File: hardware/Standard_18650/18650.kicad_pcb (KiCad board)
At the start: 2 copper layers, 109.7 x 16 mm, 57 parts, among them J2 Battery, J3 GPIO, J4 USB_B_Micro, J5 Power, J6 LEDs, J7 GPIO, Q1 BSS806N, Q2 BSS806N, Q3 BSS806N, Q4 BSS806N, SW1 Mode, SW2 Power, U1 STM32F412CGUx, U2 AP2210N-3.3TRG1, U3 BQ21040, U4 ESD7002WTT1G, Y1 32.768kHz

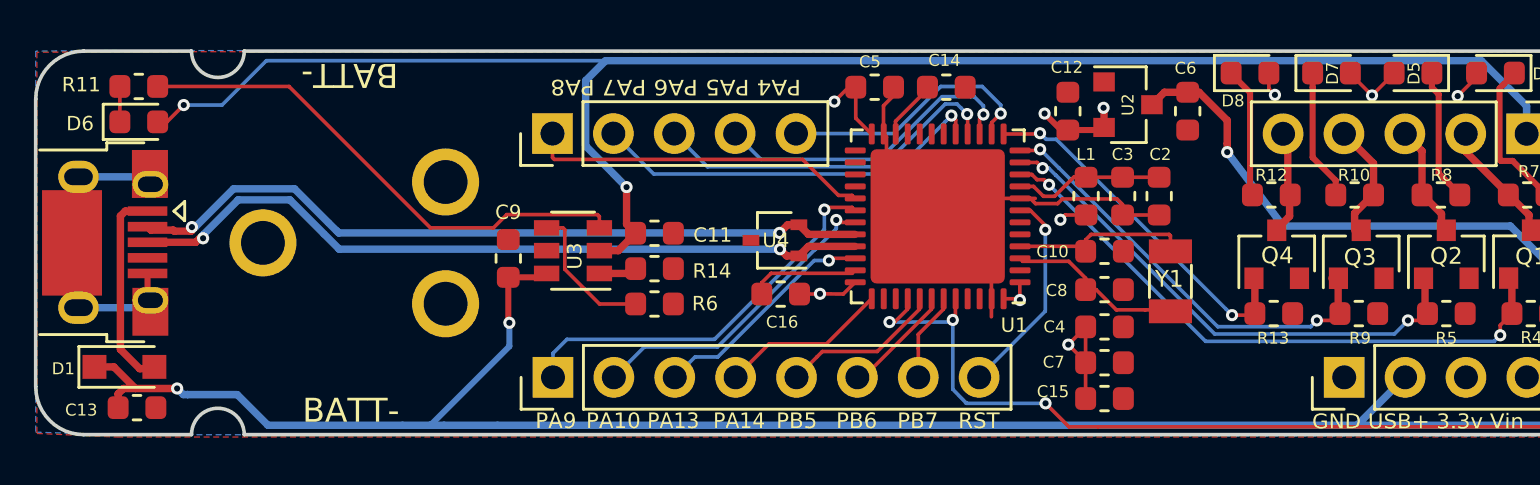
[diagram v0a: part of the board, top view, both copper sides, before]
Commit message: Add HSE crystal
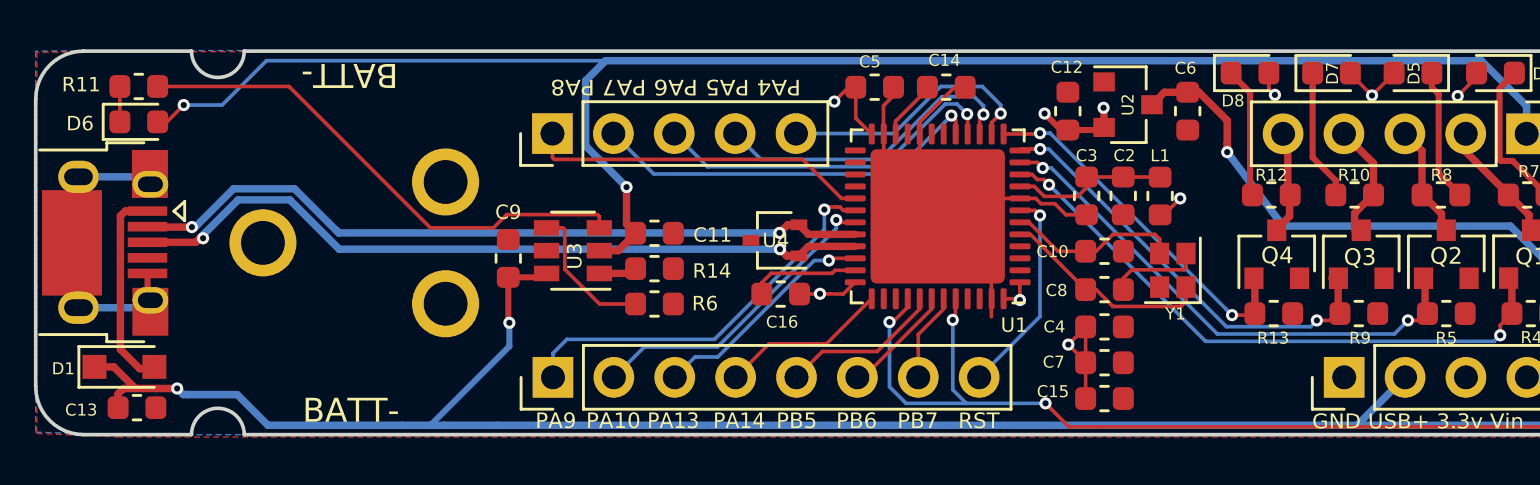
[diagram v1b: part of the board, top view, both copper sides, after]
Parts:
- C10, C8: value 7pF -> 6pF
- C11, C13, C2, C6: value 1uf -> 1uF
- C15, C16, C3, C4, C5: value 100nf -> 100nF
- Y1: value 32.768kHz -> 24Mhz; footprint Crystal:Crystal_SMD_3215-2Pin_3.2x1.5mm -> Crystal:Crystal_SMD_2016-4Pin_2.0x1.6mm
- moved L1 3.09 mm to (105.0, 98.0)
- moved C2 1.50 mm to (103.5, 98.0)
- moved C3 1.50 mm to (101.9, 98.0)
- moved Y1 0.47 mm to (105.5, 101.1), turned to 90 degrees
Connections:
- U1 pad 20: (no net) -> GND
- U1 pad 3: /XTAL1 -> (no net)
- U1 pad 4: /XTAL2 -> (no net)
- U1 pad 5: (no net) -> /XTAL1
- U1 pad 6: (no net) -> /XTAL2
- Y1 pad 2: /XTAL2 -> GND
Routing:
- net GND: track 31.8 -> 41.3 mm
- net /BUTTON: track 40.4 -> 44.0 mm
- net /XTAL1: track 7.45 -> 8.86 mm
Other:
- board text added: "rev 1.1a2"
- board text removed: "rev 1.1a"

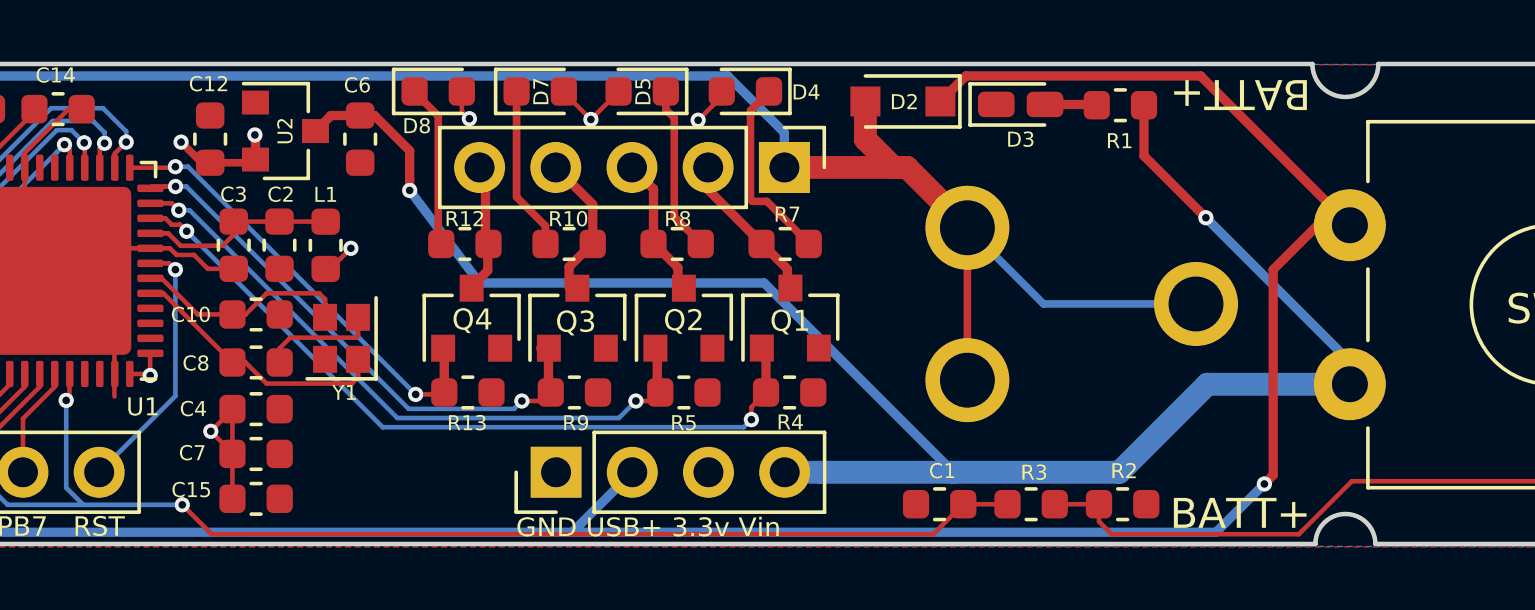
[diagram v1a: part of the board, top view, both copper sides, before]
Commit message: Add extra ground pin.
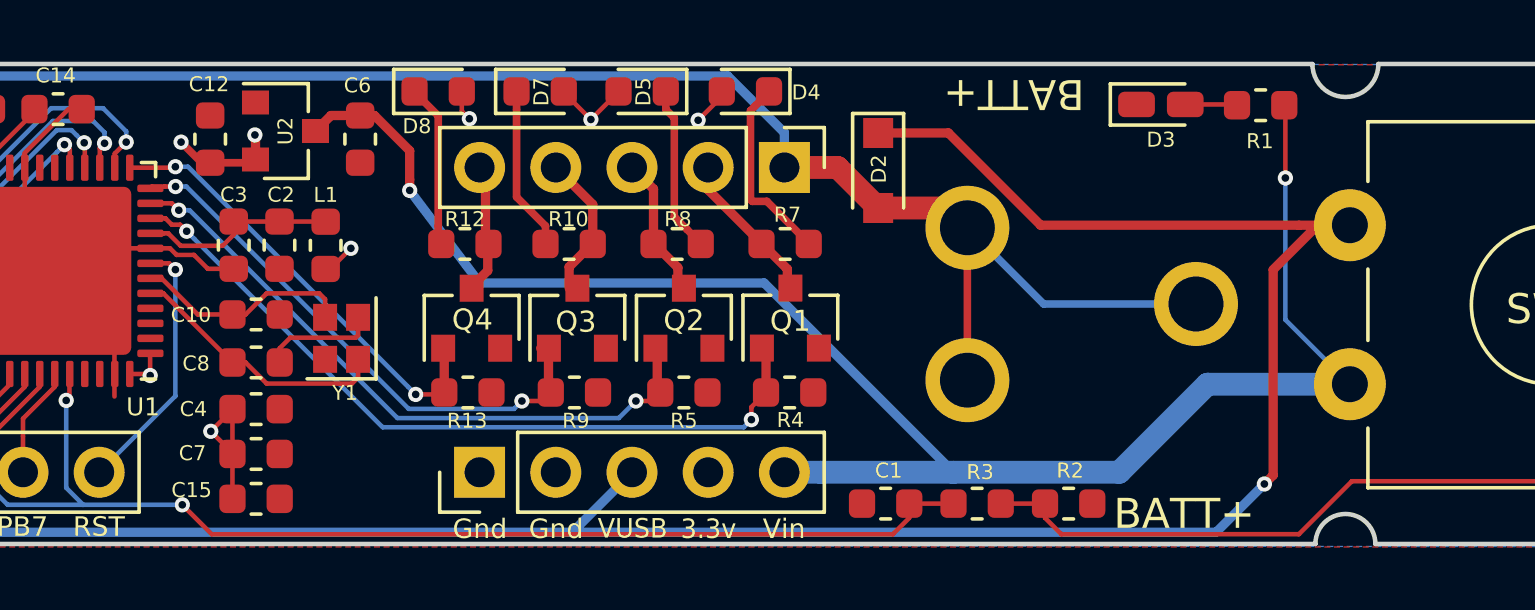
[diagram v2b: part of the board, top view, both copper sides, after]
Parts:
- J5: footprint Connector_PinHeader_2.54mm:PinHeader_1x04_P2.54mm_Vertical -> Connector_PinHeader_2.54mm:PinHeader_1x05_P2.54mm_Vertical
- moved R1 4.68 mm to (136.2, 93.4)
- moved D3 4.67 mm to (132.8, 93.3)
- moved J5 2.55 mm to (110.1, 105.6)
- moved D2 2.44 mm to (123.4, 95.5), turned to 270 degrees
- moved R3 1.80 mm to (126.7, 106.7)
- moved C1 1.80 mm to (123.7, 106.7)
- moved R2 1.80 mm to (129.8, 106.7)
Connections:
- J5 pad 2: /VUSB -> GND
- J5 pad 3: +3V3 -> /VUSB
- J5 pad 4: /VIN -> +3V3
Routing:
- net +BATT: track 94.1 -> 91.0 mm
- net /VIN: track 59.6 -> 57.7 mm
- net Net-(R2-Pad1): track 38.2 -> 40.0 mm
- net /BUTTON: track 44.0 -> 42.5 mm
- net /VUSB: track 116.5 -> 117.4 mm
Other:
- board text added: "VUSB"
- board text removed: "GND USB+ 3.3v Vin"

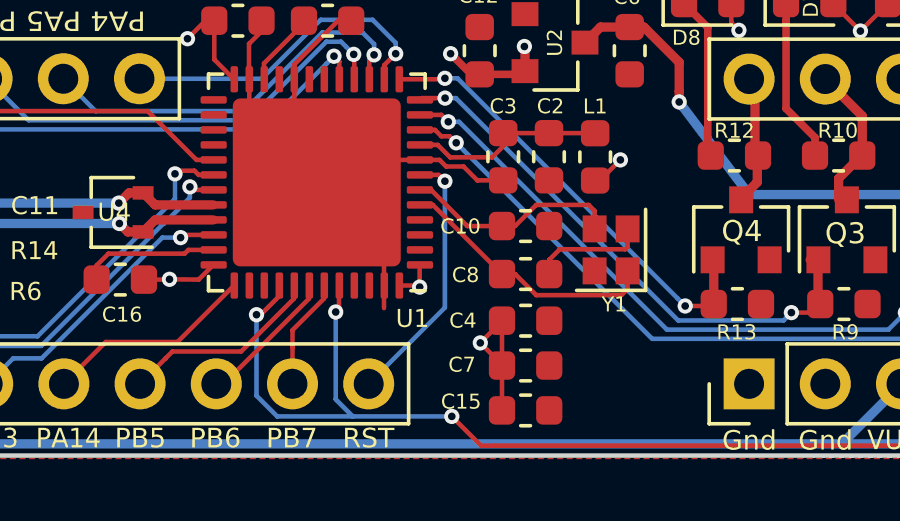
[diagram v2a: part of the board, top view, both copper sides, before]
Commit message: Updates for STM32F412
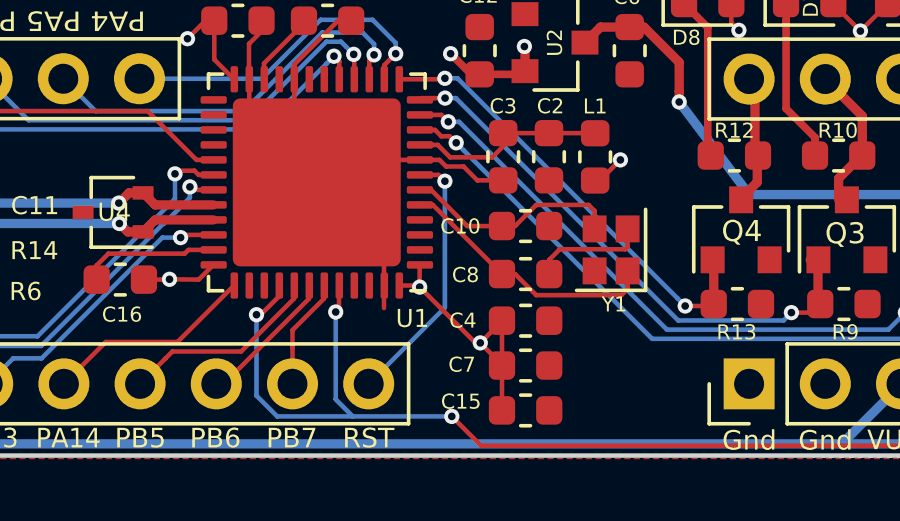
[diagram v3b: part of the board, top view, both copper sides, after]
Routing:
- net +3V3: track 24.4 -> 27.2 mm
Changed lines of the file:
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@@
     (thickness 1.6)
     (drawings 82)
-    (tracks 453)
+    (tracks 455)
     (zones 0)
     (modules 57)
@@
   )
   (setup
-    (last_trace_width 0.31)
+    (last_trace_width 0.1524)
     (user_trace_width 0.254)
     (user_trace_width 0.31)
@@
   (segment (start 105.1625 98.8325) (end 105.85 98.145) (width 0.1524) (layer F.Cu) (net 3))
   (segment (start 105.01 98.8325) (end 105.1625 98.8325) (width 0.1524) (layer F.Cu) (net 3))
+  (segment (start 101.02 104.245) (end 101.18 104.245) (width 0.1524) (layer F.Cu) (net 3))
+  (segment (start 99.16 102.385) (end 101.02 104.245) (width 0.1524) (layer F.Cu) (net 3))
   (segment (start 120.3 95.45) (end 120.3 94.29) (width 0.31) (layer B.Cu) (net 4))
   (segment (start 120.3 94.29) (end 118.41 92.4) (width 0.31) (layer B.Cu) (net 4))

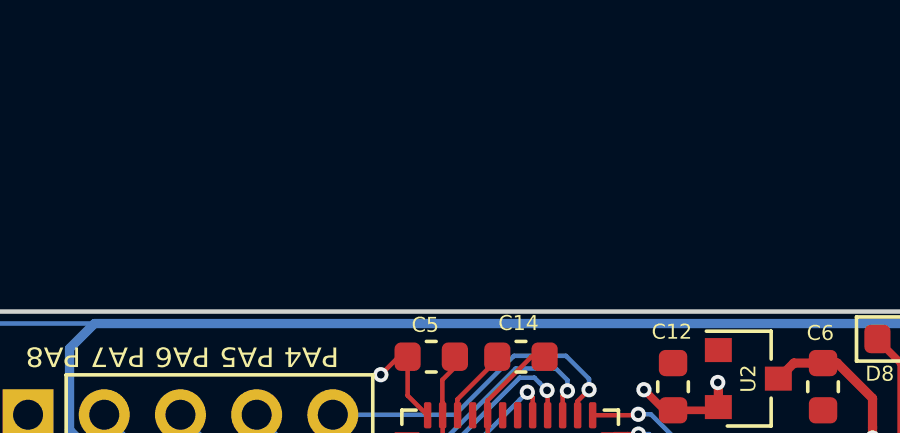
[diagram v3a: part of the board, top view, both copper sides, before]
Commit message: Add CircuitPython examples.
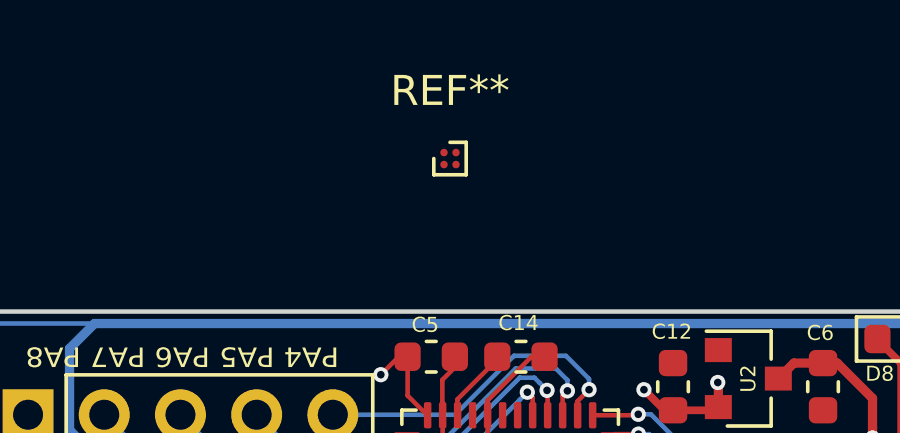
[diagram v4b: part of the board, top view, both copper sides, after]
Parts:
- added REF**: WLP-4_0.86x0.86mm_P0.4mm, Package_BGA:WLP-4_0.86x0.86mm_P0.4mm, F.Cu at (93.7, 86.9)
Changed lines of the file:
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@@
     (tracks 455)
     (zones 0)
-    (modules 57)
+    (modules 58)
     (nets 45)
   )
@@
     (add_net "Net-(R6-Pad1)")
   )
+  (module Package_BGA:WLP-4_0.86x0.86mm_P0.4mm (layer F.Cu)
+    (at 93.725 86.9)
+    (descr "WLP-4_0.86x0.86mm_P0.4mm https://pdfserv.maximintegrated.com/package_dwgs/21-0612.PDF, https://www.maximintegrated.com/en/app-notes/index.mvp/id/1891")
+    (tags WLP-4)
+    (attr smd)
+    (fp_text reference REF** (at 0 -2.25) (layer F.SilkS)
+      (effects (font (size 1 1) (thickness 0.15)))
+    )
+    (fp_text value WLP-4_0.86x0.86mm_P0.4mm (at 0 2.25) (layer F.Fab)
+      (effects (font (size 1 1) (thickness 0.15)))
+    )
+    (fp_line (start -1.43 -1.43) (end 1.43 -1.43) (layer F.CrtYd) (width 0.05))
+    (fp_line (start -1.43 1.43) (end -1.43 -1.43) (layer F.CrtYd) (width 0.05))
+    (fp_line (start 1.43 1.43) (end -1.43 1.43) (layer F.CrtYd) (width 0.05))
+    (fp_line (start 1.43 -1.43) (end 1.43 1.43) (layer F.CrtYd) (width 0.05))
+    (fp_line (start 0.54 0.54) (end 0.54 -0.54) (layer F.SilkS) (width 0.12))
+    (fp_line (start -0.54 0.54) (end 0.54 0.54) (layer F.SilkS) (width 0.12))
+    (fp_line (start -0.54 0) (end -0.54 0.54) (layer F.SilkS) (width 0.12))
+    (fp_line (start 0.54 -0.54) (end 0 -0.54) (layer F.SilkS) (width 0.12))
+    (fp_line (start -0.17 -0.43) (end -0.43 -0.17) (layer F.Fab) (width 0.1))
+    (fp_line (start -0.43 -0.16) (end -0.43 0.43) (layer F.Fab) (width 0.1))
+    (fp_line (start 0.43 -0.43) (end -0.17 -0.43) (layer F.Fab) (width 0.1))
+    (fp_line (start 0.43 0.43) (end -0.43 0.43) (layer F.Fab) (width 0.1))
+    (fp_line (start 0.43 -0.43) (end 0.43 0.43) (layer F.Fab) (width 0.1))
+    (fp_text user %R (at 0 0) (layer F.Fab)
+      (effects (font (size 0.18 0.18) (thickness 0.045)))
+    )
+    (pad B2 smd circle (at 0.2 0.2) (size 0.25 0.25) (layers F.Cu F.Paste F.Mask))
+    (pad B1 smd circle (at -0.2 0.2) (size 0.25 0.25) (layers F.Cu F.Paste F.Mask))
+    (pad A2 smd circle (at 0.2 -0.2) (size 0.25 0.25) (layers F.Cu F.Paste F.Mask))
+    (pad A1 smd circle (at -0.2 -0.2) (size 0.25 0.25) (layers F.Cu F.Paste F.Mask))
+    (model ${KISYS3DMOD}/Package_BGA.3dshapes/WLP-4_0.86x0.86mm_P0.4mm.wrl
+      (at (xyz 0 0 0))
+      (scale (xyz 1 1 1))
+      (rotate (xyz 0 0 0))
+    )
+  )
   (module Diode_SMD:D_SOD-323_HandSoldering (layer F.Cu)
